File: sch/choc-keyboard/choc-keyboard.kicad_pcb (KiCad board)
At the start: 2 copper layers, 200 x 100 mm, 81 parts, among them SW1 SW_Push, SW10 SW_Push, SW11 SW_Push, SW12 SW_Push, SW13 SW_Push, SW14 SW_Push, SW15 SW_Push, SW16 SW_Push, SW17 SW_Push, SW18 SW_Push, SW19 SW_Push, SW2 SW_Push, SW20 SW_Push, SW21 SW_Push, SW22 SW_Push, SW23 SW_Push, SW24 SW_Push, SW25 SW_Push, SW26 SW_Push, SW27 SW_Push, SW28 SW_Push, SW29 SW_Push, SW3 SW_Push, SW30 SW_Push, SW31 SW_Push, SW32 SW_Push, SW33 SW_Push, SW34 SW_Push, SW35 SW_Push, SW36 SW_Push, SW37 SW_Push, SW38 SW_Push, SW39 SW_Push, SW4 SW_Push, SW40 SW_Push, SW5 SW_Push, SW6 SW_Push, SW7 SW_Push, SW8 SW_Push, SW9 SW_Push

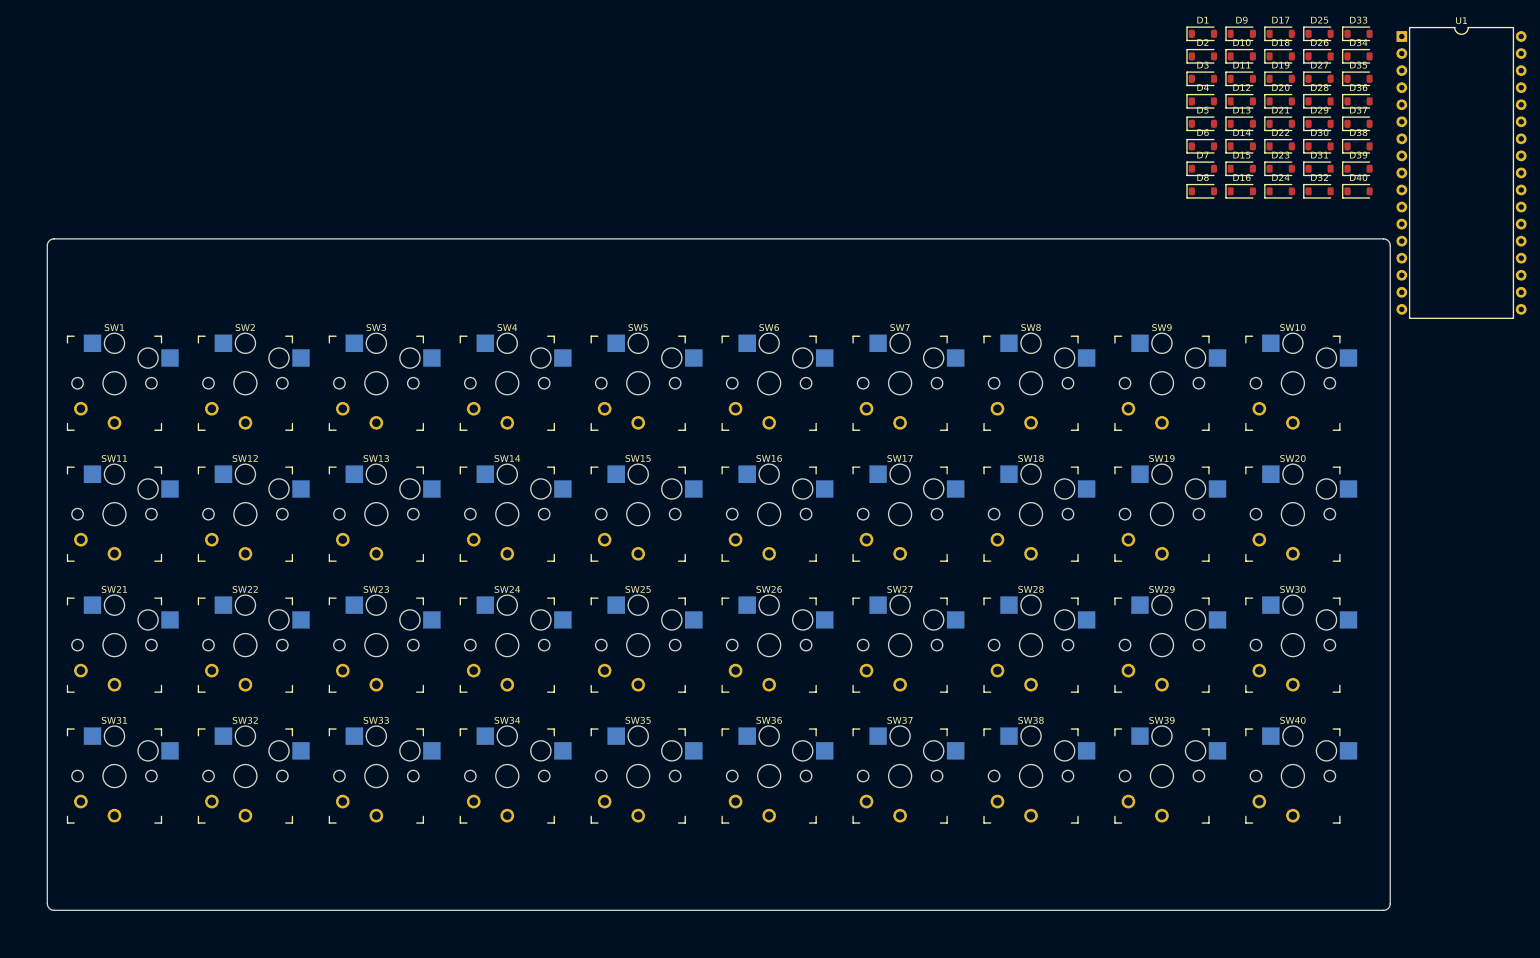
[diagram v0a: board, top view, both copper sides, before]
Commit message: 配線しながらマイコンのピン配を検討中。
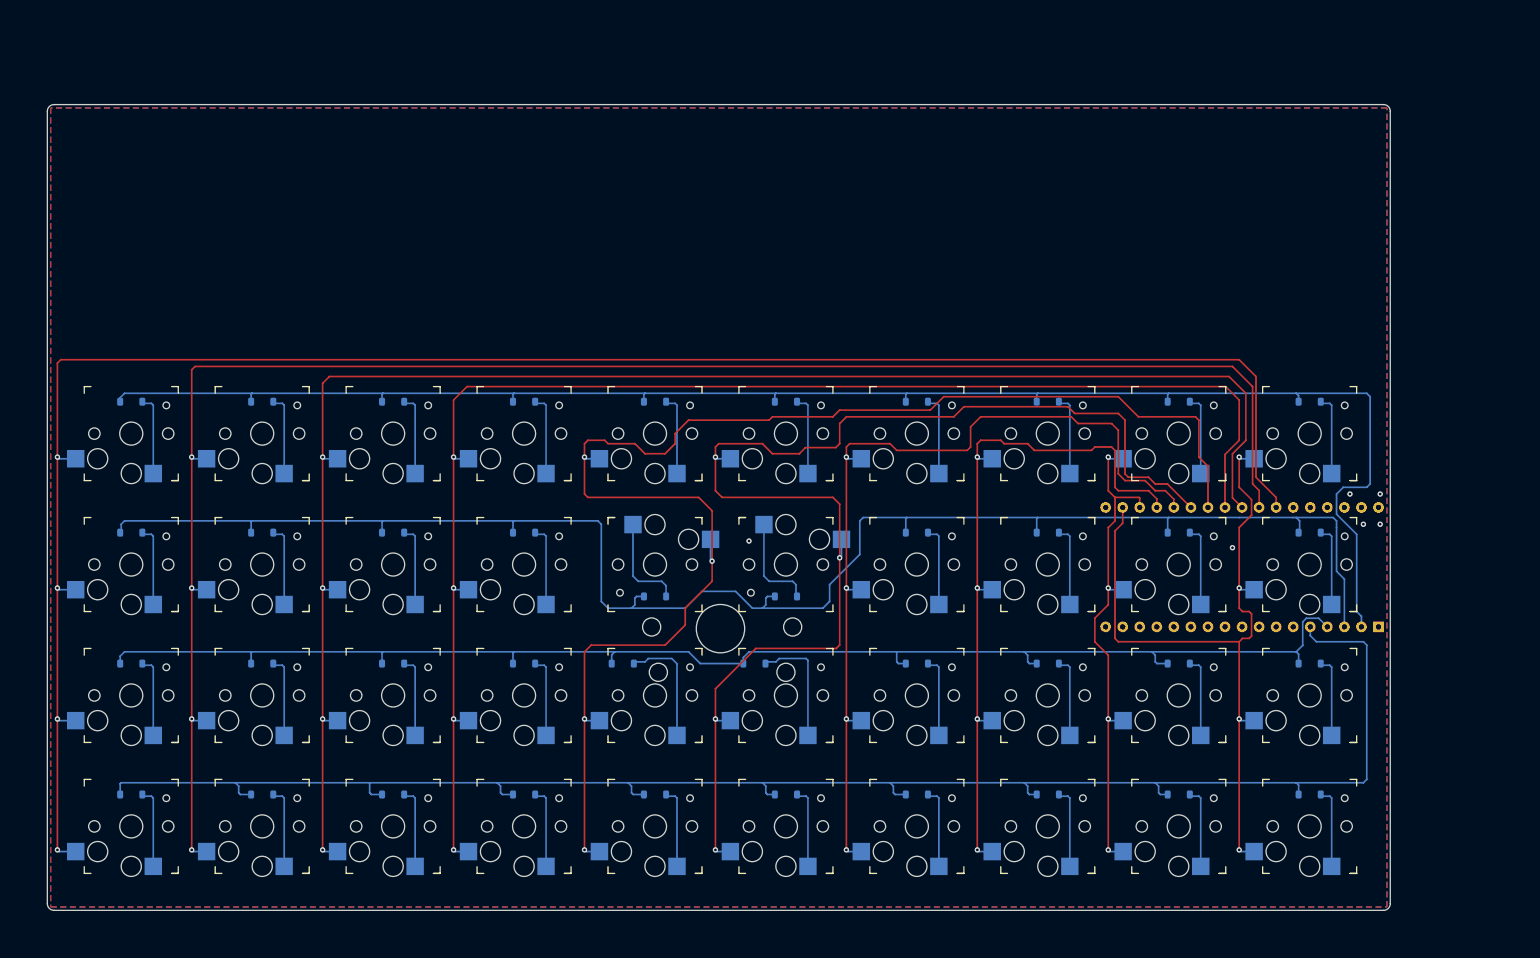
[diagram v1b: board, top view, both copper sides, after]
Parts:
- added U2: ~, trackpoint:trackpoint_t400, F.Cu at (150.2, 108.0)
- D1, D10, D11, D12, D13, D14, D15, D16, D17, D18, D19, D2, D20, D21, D22, D23, D24, D25, D26, D27, D28, D29, D3, D30, D31, D32, D33, D34, D35, D36, D37, D38, D39, D4, D40, D5, D6, D7, D8, D9, U1: moved to B.Cu
- SW1, SW10, SW11, SW12, SW13, SW14, SW15, SW16, SW17, SW18, SW19, SW2, SW20, SW21, SW22, SW23, SW24, SW25, SW26, SW27, SW28, SW29, SW3, SW30, SW31, SW32, SW33, SW34, SW35, SW36, SW37, SW38, SW39, SW4, SW40, SW5, SW6, SW7, SW8, SW9: footprint keyswitches:Kailh_socket_PG1350_optional -> keyswitches:Kailh_socket_PG1350
- moved D31 200.0 mm to (62.5, 132.8)
- moved D21 189.1 mm to (62.5, 113.2)
- moved D33 183.0 mm to (101.5, 132.8)
- moved D32 181.3 mm to (82.0, 132.8)
- moved D11 178.7 mm to (62.5, 93.8)
- moved D22 170.1 mm to (82.0, 113.2)
- moved D1 168.7 mm to (62.5, 74.2)
- moved D34 165.9 mm to (121.0, 132.8)
- moved D12 159.4 mm to (82.0, 93.8)
- moved D23 151.3 mm to (101.5, 113.2)
- moved D35 149.5 mm to (140.5, 132.8)
- moved D2 149.2 mm to (82.0, 74.2)
- moved D13 140.3 mm to (101.5, 93.8)
- moved D25 139.9 mm to (135.7, 113.2)
- moved D36 133.9 mm to (160.0, 132.8)
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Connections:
- U1 pad 1: unconnected-(U1-+5V-Pad1) -> +5V
- U1 pad 10: /COL8 -> unconnected-(U1-GPIO8-Pad10)
- U1 pad 11: /COL9 -> unconnected-(U1-GPIO9-Pad11)
- U1 pad 12: /ROW0 -> unconnected-(U1-GPIO10-Pad12)
- U1 pad 13: /ROW1 -> unconnected-(U1-GPIO11-Pad13)
- U1 pad 14: /ROW2 -> unconnected-(U1-GPIO12-Pad14)
- U1 pad 15: /ROW3 -> unconnected-(U1-GPIO13-Pad15)
- U1 pad 19: unconnected-(U1-GPIO16-Pad19) -> /COL9
- U1 pad 2: /COL0 -> /ROW0
- U1 pad 20: unconnected-(U1-GPIO17-Pad20) -> /COL8
- U1 pad 21: unconnected-(U1-GPIO18-Pad21) -> /COL7
- U1 pad 22: unconnected-(U1-GPIO19-Pad22) -> /COL6
- U1 pad 23: unconnected-(U1-GPIO20-Pad23) -> /COL5
- U1 pad 24: unconnected-(U1-GPIO21-Pad24) -> /COL4
- U1 pad 25: unconnected-(U1-GPIO22-Pad25) -> /COL3
- U1 pad 26: unconnected-(U1-GPIO23-Pad26) -> /COL2
- U1 pad 27: unconnected-(U1-GPIO24-Pad27) -> /COL1
- U1 pad 28: unconnected-(U1-GPIO25-Pad28) -> /COL0
- U1 pad 3: /COL1 -> /ROW1
- U1 pad 4: /COL2 -> /ROW2
- U1 pad 5: /COL3 -> /ROW3
- U1 pad 6: /COL4 -> unconnected-(U1-GPIO4-Pad6)
- U1 pad 7: /COL5 -> unconnected-(U1-GPIO5-Pad7)
- U1 pad 8: /COL6 -> unconnected-(U1-GPIO6-Pad8)
- U1 pad 9: /COL7 -> unconnected-(U1-GPIO7-Pad9)
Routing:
- net /COL0: track 0.00 -> 284.3 mm, vias 0 -> 4
- net /COL1: track 0.00 -> 258.7 mm, vias 0 -> 4
- net /ROW3: track 0.00 -> 247.3 mm
- net /ROW1: track 0.00 -> 244.4 mm
- net /ROW0: track 0.00 -> 239.1 mm
- net /COL2: track 0.00 -> 236.2 mm, vias 0 -> 4
- net /COL4: track 0.00 -> 214.6 mm, vias 0 -> 4
- net /COL3: track 0.00 -> 211.8 mm, vias 0 -> 4
- net /ROW2: track 0.00 -> 206.8 mm
- net /COL5: track 0.00 -> 189.1 mm, vias 0 -> 4
- net /COL6: track 0.00 -> 132.7 mm, vias 0 -> 4
- net /COL9: track 0.00 -> 110.7 mm, vias 0 -> 4
- net /COL7: track 0.00 -> 105.3 mm, vias 0 -> 4
- net /COL8: track 0.00 -> 75.4 mm, vias 0 -> 4
- net Net-(D26-A): track 0.00 -> 17.9 mm
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- added copper zone on B.Cu, net GND
- added copper zone on F.Cu, net GND
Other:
- board size 200 x 100 mm -> 200 x 120 mm

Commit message: ネジ穴のぶん基板を大きくしました。
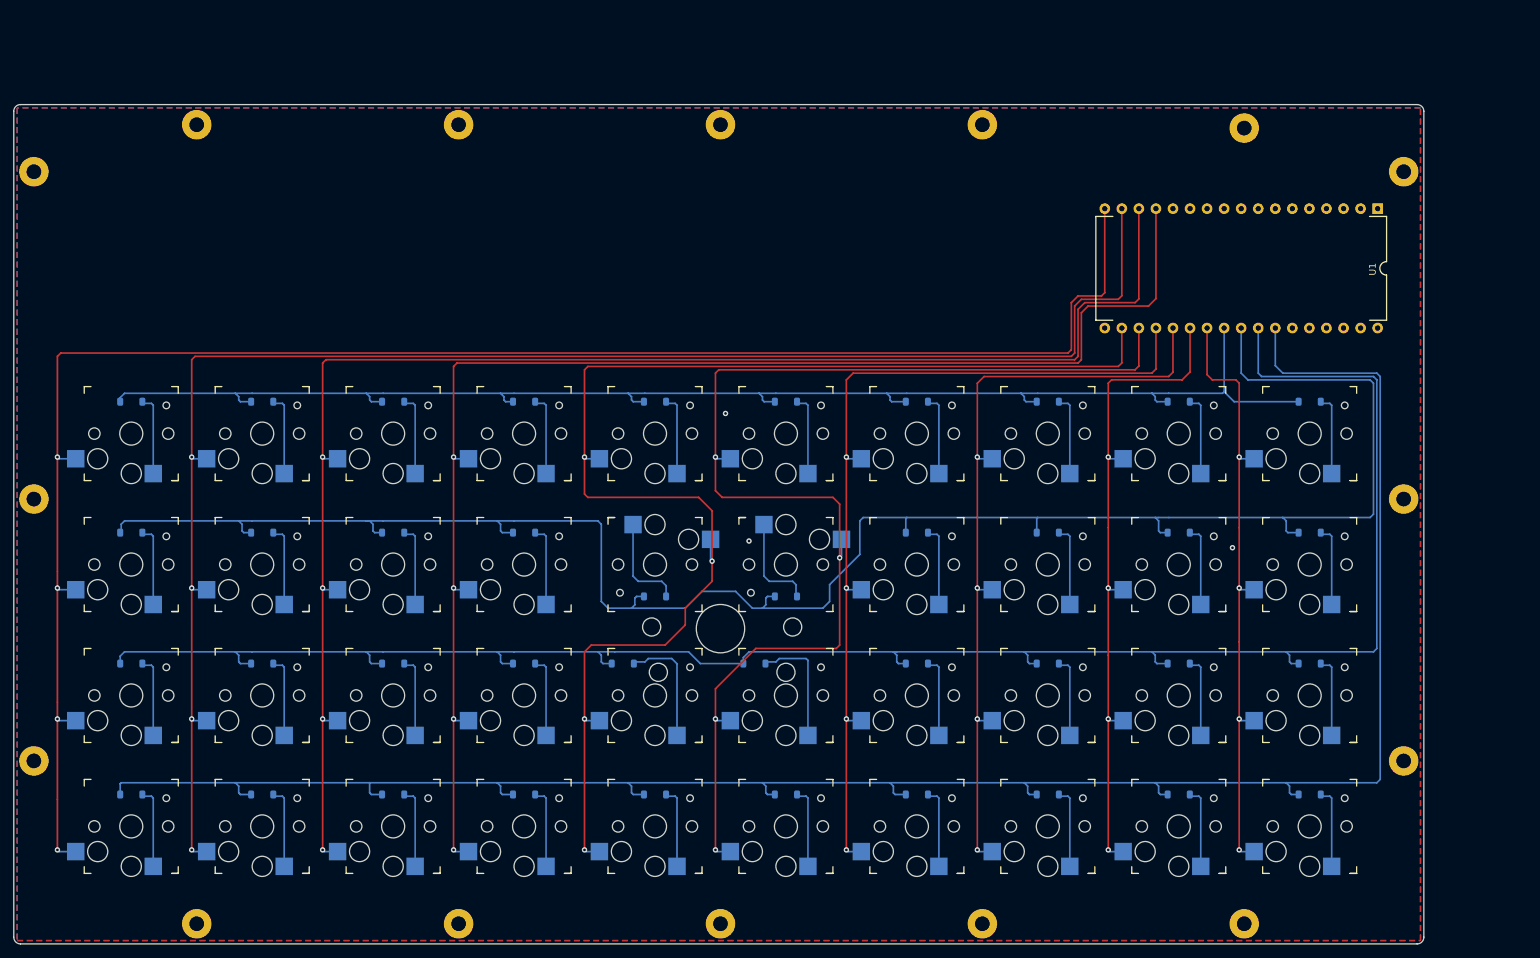
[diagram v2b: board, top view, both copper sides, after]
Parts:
- added H1: MountingHole_Pad, MountingHole:MountingHole_2.2mm_M2_Pad, F.Cu at (72.2, 33.0)
- added H10: MountingHole_Pad, MountingHole:MountingHole_2.2mm_M2_Pad, F.Cu at (228.2, 152.0)
- added H11: MountingHole_Pad, MountingHole:MountingHole_2.2mm_M2_Pad, F.Cu at (48.0, 88.8)
- added H12: MountingHole_Pad, MountingHole:MountingHole_2.2mm_M2_Pad, F.Cu at (48.0, 127.8)
- added H13: MountingHole_Pad, MountingHole:MountingHole_2.2mm_M2_Pad, F.Cu at (252.0, 127.8)
- added H14: MountingHole_Pad, MountingHole:MountingHole_2.2mm_M2_Pad, F.Cu at (252.0, 40.0)
- added H15: MountingHole_Pad, MountingHole:MountingHole_2.2mm_M2_Pad, F.Cu at (48.0, 40.0)
- added H16: MountingHole_Pad, MountingHole:MountingHole_2.2mm_M2_Pad, F.Cu at (228.2, 33.5)
- added H2: MountingHole_Pad, MountingHole:MountingHole_2.2mm_M2_Pad, F.Cu at (111.2, 33.0)
- added H3: MountingHole_Pad, MountingHole:MountingHole_2.2mm_M2_Pad, F.Cu at (150.2, 33.0)
- added H4: MountingHole_Pad, MountingHole:MountingHole_2.2mm_M2_Pad, F.Cu at (189.2, 33.0)
- added H5: MountingHole_Pad, MountingHole:MountingHole_2.2mm_M2_Pad, F.Cu at (252.0, 88.8)
- added H6: MountingHole_Pad, MountingHole:MountingHole_2.2mm_M2_Pad, F.Cu at (72.2, 152.0)
- added H7: MountingHole_Pad, MountingHole:MountingHole_2.2mm_M2_Pad, F.Cu at (111.2, 152.0)
- added H8: MountingHole_Pad, MountingHole:MountingHole_2.2mm_M2_Pad, F.Cu at (150.2, 152.0)
- added H9: MountingHole_Pad, MountingHole:MountingHole_2.2mm_M2_Pad, F.Cu at (189.2, 152.0)
- U1: moved to F.Cu
- moved U1 62.3 mm to (248.1, 45.5), turned to -90 degrees
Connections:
- U1 pad 14: unconnected-(U1-GPIO12-Pad14) -> /COL3
- U1 pad 15: unconnected-(U1-GPIO13-Pad15) -> /COL2
- U1 pad 16: unconnected-(U1-GPIO14-Pad16) -> /COL1
- U1 pad 17: unconnected-(U1-GPIO15-Pad17) -> /COL0
- U1 pad 19: /COL9 -> /COL4
- U1 pad 2: /ROW0 -> unconnected-(U1-GPIO0-Pad2)
- U1 pad 20: /COL8 -> /COL5
- U1 pad 21: /COL7 -> /COL6
- U1 pad 22: /COL6 -> /COL7
- U1 pad 23: /COL5 -> /COL8
- U1 pad 24: /COL4 -> /COL9
- U1 pad 25: /COL3 -> /ROW0
- U1 pad 26: /COL2 -> /ROW1
- U1 pad 27: /COL1 -> /ROW2
- U1 pad 28: /COL0 -> /ROW3
- U1 pad 3: /ROW1 -> unconnected-(U1-GPIO1-Pad3)
- U1 pad 4: /ROW2 -> unconnected-(U1-GPIO2-Pad4)
- U1 pad 5: /ROW3 -> unconnected-(U1-GPIO3-Pad5)
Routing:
- net /ROW2: track 206.8 -> 283.0 mm
- net /ROW3: track 247.3 -> 302.1 mm
- net /ROW1: track 244.4 -> 288.2 mm
- net /ROW0: track 239.1 -> 211.9 mm
- net /COL0: track 284.3 -> 261.3 mm
- net /COL8: track 75.4 -> 98.2 mm
- net /COL9: track 110.7 -> 91.1 mm
- net /COL1: track 258.7 -> 241.9 mm
- net /COL4: track 214.6 -> 199.3 mm
- net /COL2: track 236.2 -> 224.9 mm
- net /COL7: track 105.3 -> 115.2 mm
- net /COL5: track 189.1 -> 182.0 mm
- net /COL3: track 211.8 -> 207.6 mm
- net GND: vias 6 -> 3
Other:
- board size 200 x 120 mm -> 210 x 125 mm

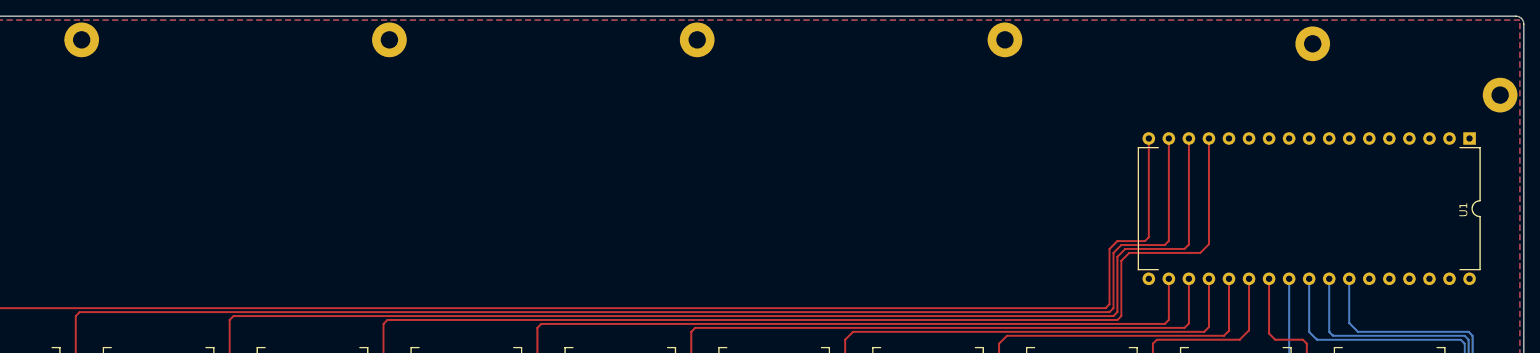
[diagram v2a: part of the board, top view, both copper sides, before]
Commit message: キャラクタLCDを追加。
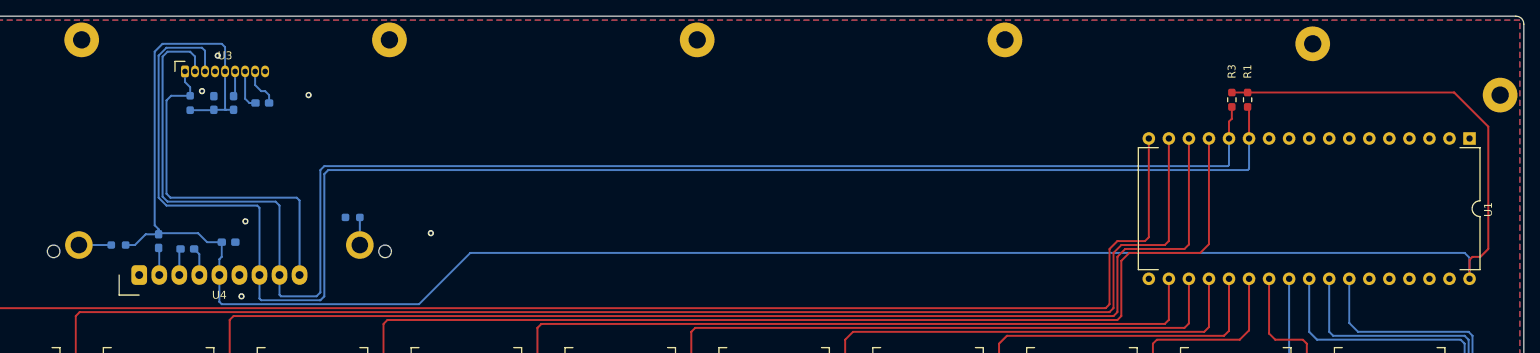
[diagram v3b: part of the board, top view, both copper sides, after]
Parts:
- added C1: 1u, Capacitor_SMD:C_0603_1608Metric_Pad1.08x0.95mm_HandSolder, B.Cu at (89.0, 41.0)
- added C2: 1u, Capacitor_SMD:C_0603_1608Metric_Pad1.08x0.95mm_HandSolder, B.Cu at (90.9, 58.6)
- added C3: 1u, Capacitor_SMD:C_0603_1608Metric_Pad1.08x0.95mm_HandSolder, B.Cu at (91.5, 41.0)
- added C4: 1u, Capacitor_SMD:C_0603_1608Metric_Pad1.08x0.95mm_HandSolder, B.Cu at (82.0, 58.5)
- added C5: 1u, Capacitor_SMD:C_0603_1608Metric_Pad1.08x0.95mm_HandSolder, B.Cu at (95.1, 41.0)
- added C6: 1u, Capacitor_SMD:C_0603_1608Metric_Pad1.08x0.95mm_HandSolder, B.Cu at (85.6, 59.5)
- added R1: 10k, Resistor_SMD:R_0603_1608Metric_Pad0.98x0.95mm_HandSolder, F.Cu at (220.0, 40.6)
- added R3: 10k, Resistor_SMD:R_0603_1608Metric_Pad0.98x0.95mm_HandSolder, F.Cu at (218.0, 40.6)
- added R5: 10k, Resistor_SMD:R_0603_1608Metric_Pad0.98x0.95mm_HandSolder, B.Cu at (86.0, 41.0)
- added R7: 1k, Resistor_SMD:R_0603_1608Metric_Pad0.98x0.95mm_HandSolder, B.Cu at (76.9, 59.0)
- added R8: 0, Resistor_SMD:R_0603_1608Metric_Pad0.98x0.95mm_HandSolder, B.Cu at (106.6, 55.5)
- added U3: AQM1602XA-RN-GBW, AQM1602:AQM1602XA-RN-GBW, F.Cu at (90.4, 37.0)
- added U4: AQM1602Y-NLW-FBW, AQM1602:AQM1602Y-NLW-FBW, F.Cu at (89.7, 62.8)
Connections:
- U1 pad 12: unconnected-(U1-GPIO10-Pad12) -> /LCD_I2C_SDA
- U1 pad 13: unconnected-(U1-GPIO11-Pad13) -> /LCD_I2C_SCL
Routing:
- net +3.3V: track 0.00 -> 286.6 mm
- net /LCD_I2C_SDA: track 0.00 -> 201.3 mm
- net /LCD_I2C_SCL: track 0.00 -> 194.7 mm
- net Net-(U3-RES_N): track 0.00 -> 45.1 mm
- net Net-(U3-CAP1N): track 0.00 -> 5.03 mm
- net Net-(U3-CAP1P): track 0.00 -> 5.00 mm
- net Net-(U4-LED_A): track 0.00 -> 4.10 mm
- net Net-(U4-CAP1P): track 0.00 -> 3.57 mm
- net Net-(U4-LED_K): track 0.00 -> 3.50 mm
- net Net-(U4-VOUT): track 0.00 -> 3.47 mm
- net Net-(U4-CAP1N): track 0.00 -> 3.36 mm
- net Net-(U3-VOUT): track 0.00 -> 3.22 mm
- net GND: track 0.00 -> 0.21 mm, vias 3 -> 9
